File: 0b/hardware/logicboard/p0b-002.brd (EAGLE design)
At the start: 70 x 41 mm, 30 parts, among them IC1 7404D, IC4 LTC485S, IC5 LTC485S, J0 DC5V, J7 DIN5, J9 DIN5, X7 NELTRON-7810-XPXC

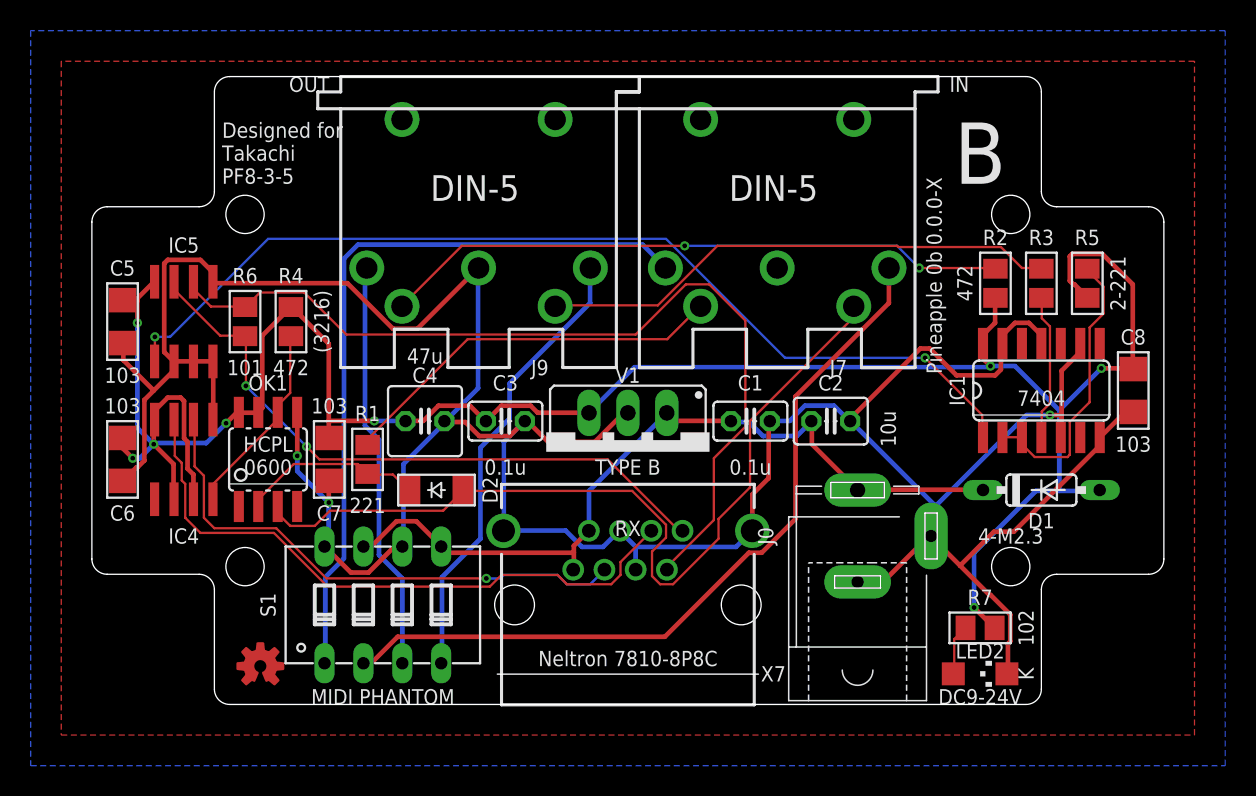
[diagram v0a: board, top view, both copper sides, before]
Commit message: Added Direct-5V resistor pattern.
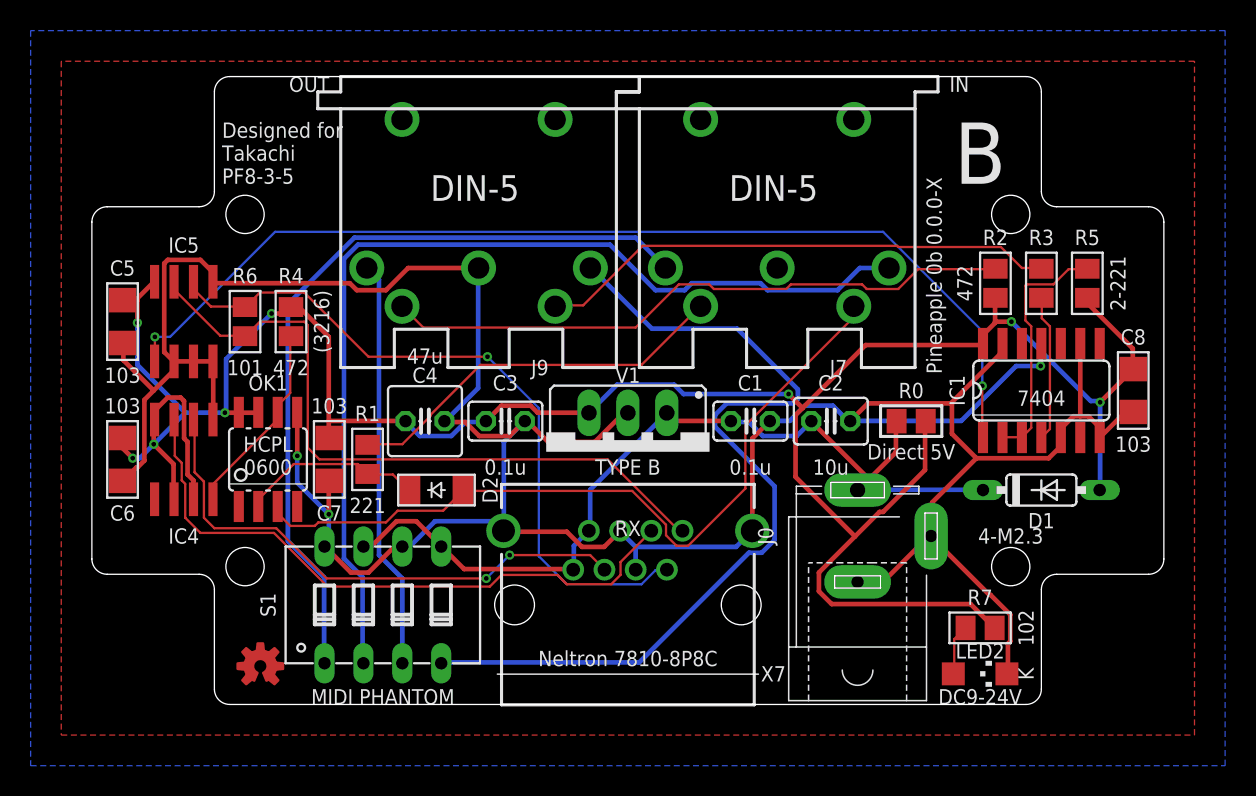
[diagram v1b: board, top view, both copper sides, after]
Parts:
- added R0: Inf, rcl:M2012
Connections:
- net V+: now also R0.1
- net VCC: now also R0.2
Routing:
- net MIDIOUTV+: track 29.8 -> 58.2 mm
- net VCC: track 153.3 -> 168.0 mm
- net MIDIINV+: track 51.0 -> 65.1 mm
- net RX+: track 59.3 -> 46.2 mm, vias 0 -> 1
- net GND: track 224.9 -> 215.3 mm
- net V+: track 52.5 -> 59.0 mm
- net MIRTN: track 56.5 -> 50.6 mm
- net RX: track 64.6 -> 68.2 mm
- net RX-: track 42.1 -> 45.7 mm, vias 2 -> 0
- net MIDIINGND: track 49.0 -> 51.7 mm
- net NMIDIOUT: track 18.8 -> 16.1 mm
- net MOSND: track 41.0 -> 41.4 mm, vias 2 -> 0
- net TX+: track 35.3 -> 35.6 mm, vias 1 -> 2
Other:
- board text added: "Direct 5V"

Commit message: Pinhead.
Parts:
- removed R0: Inf, rcl:M2012
- added JP1: (no value), pinhead:1X02
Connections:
- net V+: now also JP1.1; no longer R0.1
- net VCC: now also JP1.2; no longer R0.2
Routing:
- net MIDIOUTV+: track 58.2 -> 29.8 mm
- net MIDIINV+: track 65.1 -> 50.1 mm
- net MIDIOUTGND: track 26.8 -> 32.9 mm
- net RX-: track 45.7 -> 50.5 mm
- net GND: track 215.3 -> 211.7 mm
- net MIRTN: track 50.6 -> 53.8 mm, vias 0 -> 1
- net RX: track 68.2 -> 66.2 mm
- net V+: track 59.0 -> 57.7 mm
- net MIDIINGND: track 51.7 -> 52.9 mm
- net RX+: track 46.2 -> 47.2 mm, vias 1 -> 2
- net MISND: track 25.5 -> 26.3 mm
- net MOSND: track 41.4 -> 42.2 mm
- net TX+: track 35.6 -> 34.9 mm, vias 2 -> 0
- net TX-: track 41.5 -> 40.9 mm
- net VCC: track 168.0 -> 168.6 mm
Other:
- board text added: "485"
- board text removed: "RX"

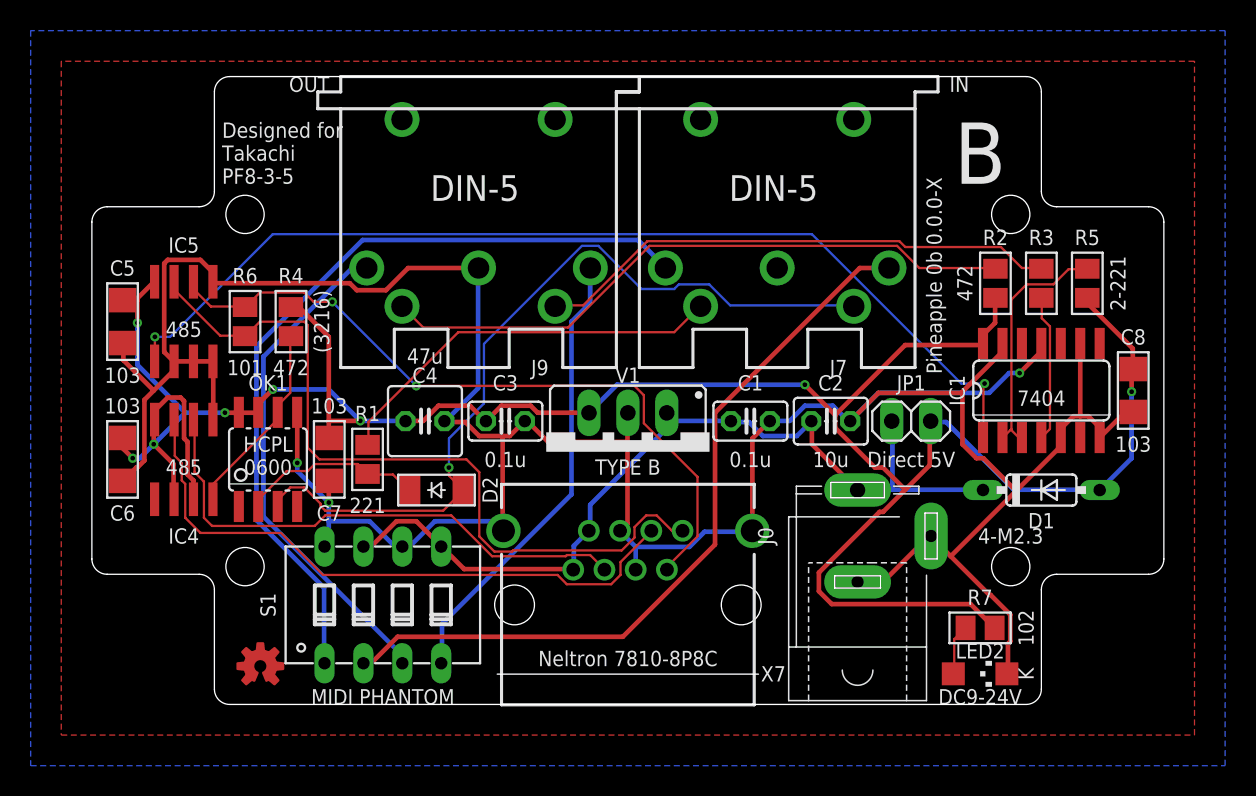
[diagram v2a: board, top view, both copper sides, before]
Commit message: Added PoE R.
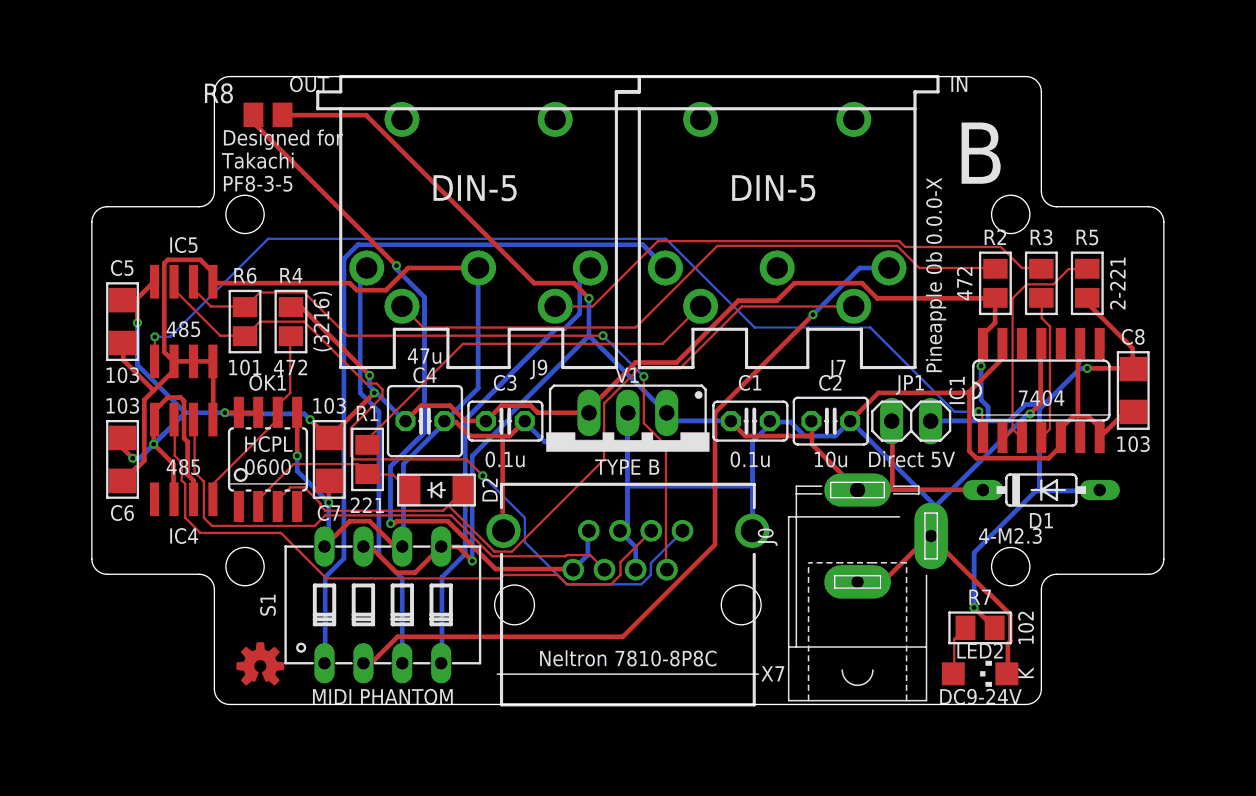
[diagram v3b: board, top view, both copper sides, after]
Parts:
- added R8: 0, rcl:M2012
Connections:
- new net POE: R8.1, X7.7, X7.8
- net V+: now also R8.2; no longer X7.7, X7.8
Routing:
- net POE: track 0.00 -> 48.5 mm, vias 0 -> 2
- net V+: track 57.7 -> 89.9 mm, vias 0 -> 2
- net VCC: track 168.6 -> 154.7 mm, vias 8 -> 10
- net GND: track 211.7 -> 217.5 mm
- net MIDIOUTGND: track 32.9 -> 27.1 mm
- net MIDIINGND: track 52.9 -> 49.0 mm
- net MIRTN: track 53.8 -> 50.7 mm, vias 1 -> 0
- net RX: track 66.2 -> 64.6 mm
- net RX+: track 47.2 -> 46.3 mm
- net MISND: track 26.3 -> 25.7 mm
- net RX-: track 50.5 -> 50.8 mm, vias 0 -> 1
- net MIDIINV+: vias 0 -> 1
- removed copper zone on layer 1, net GND
- removed copper zone on layer 16, net GND

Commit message: Pinhead.
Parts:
- added JP2: (no value), pinhead:1X02
- R8: value 0 -> 20
- moved R8 6.96 mm to (14.0, 32.0), turned to 270 degrees
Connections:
- new net POERAW: JP2.1, R8.1
- net POE: now also JP2.2; no longer R8.1
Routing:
- net VCC: track 154.7 -> 141.8 mm, vias 10 -> 9
- net V+: track 89.9 -> 78.1 mm, vias 2 -> 1
- net RX+: track 46.3 -> 55.5 mm, vias 2 -> 0
- net POE: track 48.5 -> 55.7 mm, vias 2 -> 0
- net POERAW: track 0.00 -> 6.62 mm
- net GND: track 217.5 -> 222.4 mm, vias 3 -> 5
- net MIRTN: track 50.7 -> 54.5 mm, vias 0 -> 1
- net TX+: track 34.9 -> 37.9 mm
- net TX-: track 41.1 -> 42.7 mm, vias 0 -> 2
- net MOSND: track 42.2 -> 40.5 mm, vias 0 -> 2
- net MIDIOUTV+: track 30.2 -> 31.0 mm
- net TX: track 12.8 -> 13.5 mm
- net MIDIINV+: track 50.1 -> 50.5 mm, vias 1 -> 0
- net RX-: track 50.8 -> 51.2 mm, vias 1 -> 3
- net MORTN: track 34.3 -> 34.0 mm, vias 0 -> 1
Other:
- board text added: "(2012)"
- board text added: "20"
- board text added: "PoE"
- board text removed: "(3216)"
